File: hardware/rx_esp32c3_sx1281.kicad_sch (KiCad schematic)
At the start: 43 parts, among them U21 SX1281IMLTRT, U22 ESP32-C3, U23 TLV75533PDQNR, X2 CJ17-400001010B20

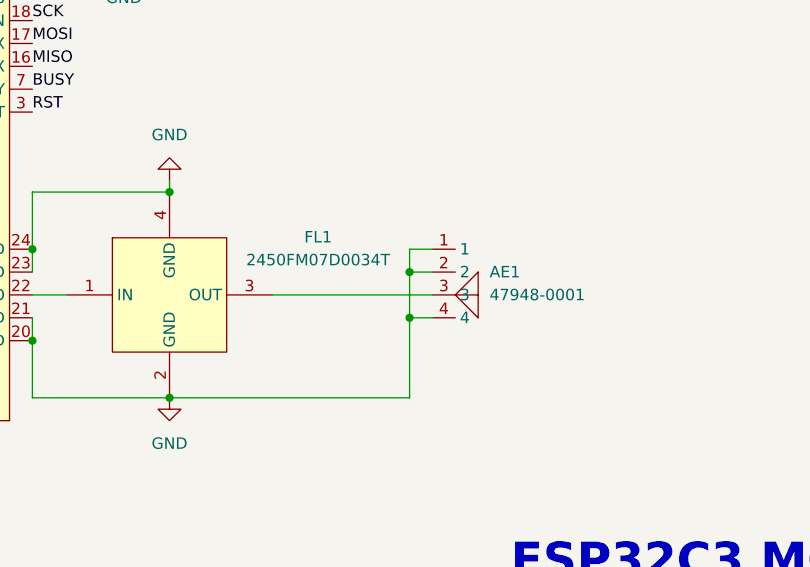
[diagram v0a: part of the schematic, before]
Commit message: Base: routing progress (~60%), netclass clearances relaxed
VBAT/Phase/Power/RF clearance lowered toward the 0.09 line standard; the
2 oz outer rule in the DRU still enforces 0.16 on F/B.Cu. Schematic sheets
resaved by eeschema, no circuit change.
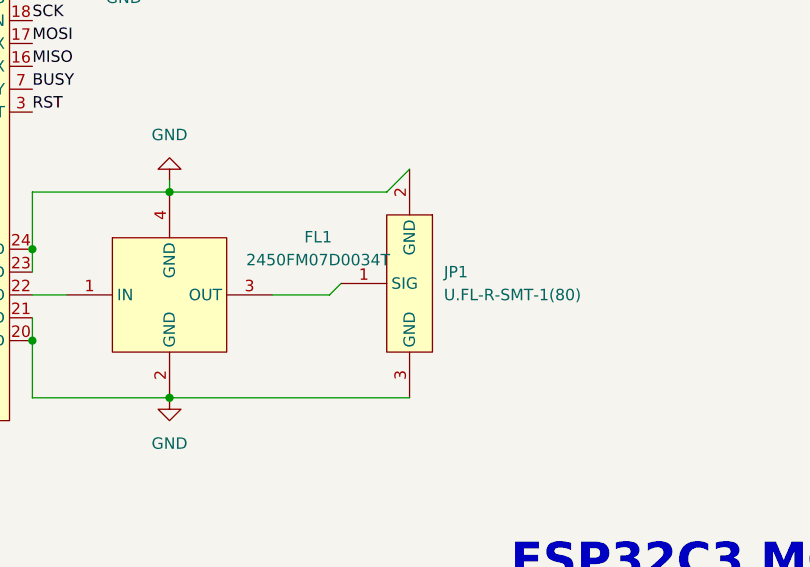
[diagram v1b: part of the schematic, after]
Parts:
- removed AE1: 47948-0001, OpenRX-Shared:ANT-SMD_47948-0001, symbol OpenRX-Shared:47948-0001
- added JP1: U.FL-R-SMT-1(80), OpenDrone:RF-SMD_FRF05002-JSS103M, symbol OpenDrone:U.FL-R-SMT-1(80)
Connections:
- net GND: now also JP1.2 (GND), JP1.3 (GND)
- net at FL1.3 (OUT): now also JP1.1 (SIG)
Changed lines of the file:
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@@
 	)
 	(junction
-		(at 185.42 119.38)
-		(diameter 0)
-		(color 0 0 0 0)
-	)
-	(junction
 		(at 273.05 93.98)
 		(diameter 0)
@@
 	)
 	(junction
-		(at 185.42 114.3)
-		(diameter 0)
-		(color 0 0 0 0)
-	)
-	(junction
 		(at 91.44 81.28)
 		(diameter 0)
@@
 	(wire
 		(pts
-			(xy 170.18 116.84) (xy 187.96 116.84)
-		)
-		(stroke
-			(width 0)
-			(type default)
-		)
-	)
-	(wire
-		(pts
 			(xy 279.4 93.98) (xy 279.4 96.52)
 		)
@@
 	(wire
 		(pts
-			(xy 185.42 114.3) (xy 185.42 119.38)
-		)
-		(stroke
-			(width 0)
-			(type default)
-		)
-	)
-	(wire
-		(pts
 			(xy 167.64 233.68) (xy 199.39 233.68)
 		)
@@
 	(wire
 		(pts
+			(xy 158.75 105.41) (xy 182.88 105.41)
+		)
+		(stroke
+			(width 0)
+			(type default)
+		)
+	)
+	(wire
+		(pts
 			(xy 77.47 71.12) (xy 80.01 71.12)
 		)
@@
 	(wire
 		(pts
+			(xy 170.18 116.84) (xy 176.53 116.84)
+		)
+		(stroke
+			(width 0)
+			(type default)
+		)
+	)
+	(wire
+		(pts
 			(xy 273.05 93.98) (xy 273.05 95.25)
 		)
@@
 	(wire
 		(pts
-			(xy 185.42 119.38) (xy 185.42 128.27)
-		)
-		(stroke
-			(width 0)
-			(type default)
-		)
-	)
-	(wire
-		(pts
 			(xy 212.09 195.58) (xy 212.09 179.07)
 		)
@@
 	(wire
 		(pts
-			(xy 261.62 93.98) (xy 273.05 93.98)
+			(xy 182.88 105.41) (xy 185.42 102.87)
 		)
 		(stroke
@@
 	(wire
 		(pts
-			(xy 264.16 180.34) (xy 264.16 179.07)
+			(xy 261.62 93.98) (xy 273.05 93.98)
 		)
 		(stroke
@@
 	(wire
 		(pts
-			(xy 187.96 111.76) (xy 185.42 111.76)
+			(xy 264.16 180.34) (xy 264.16 179.07)
 		)
 		(stroke
@@
 	(wire
 		(pts
-			(xy 187.96 114.3) (xy 185.42 114.3)
+			(xy 273.05 104.14) (xy 287.02 104.14)
 		)
 		(stroke
@@
 	(wire
 		(pts
-			(xy 273.05 104.14) (xy 287.02 104.14)
+			(xy 303.53 104.14) (xy 303.53 102.87)
 		)
 		(stroke
@@
 	(wire
 		(pts
-			(xy 303.53 104.14) (xy 303.53 102.87)
+			(xy 107.95 71.12) (xy 91.44 71.12)
 		)
 		(stroke
@@
 	(wire
 		(pts
-			(xy 107.95 71.12) (xy 91.44 71.12)
+			(xy 245.11 215.9) (xy 254 215.9)
 		)
 		(stroke
@@
 	(wire
 		(pts
-			(xy 245.11 215.9) (xy 254 215.9)
+			(xy 83.82 104.14) (xy 83.82 116.84)
 		)
 		(stroke
@@
 	(wire
 		(pts
-			(xy 83.82 104.14) (xy 83.82 116.84)
+			(xy 176.53 116.84) (xy 177.8 115.57)
 		)
 		(stroke
@@
 	(wire
 		(pts
-			(xy 185.42 111.76) (xy 185.42 114.3)
-		)
-		(stroke
-			(width 0)
-			(type default)
-		)
-	)
-	(wire
-		(pts
 			(xy 261.62 95.25) (xy 261.62 93.98)
 		)
@@
 	(wire
 		(pts
-			(xy 185.42 119.38) (xy 187.96 119.38)
-		)
-		(stroke
-			(width 0)
-			(type default)
-		)
-	)
-	(wire
-		(pts
 			(xy 181.61 186.69) (xy 168.91 186.69)
 		)
@@
 	)
 	(symbol
+		(lib_id "OpenDrone:U.FL-R-SMT-1(80)")
+		(at 182.88 115.57 270)
+		(unit 1)
+		(body_style 1)
+		(exclude_from_sim no)
+		(in_bom yes)
+		(on_board yes)
+		(in_pos_files yes)
+		(dnp no)
+		(fields_autoplaced yes)
+		(property "Reference" "JP1"
+			(at 189.23 114.2999 90)
+			(show_name no)
+			(do_not_autoplace no)
+			(effects
+				(font
+					(size 1.27 1.27)
+				)
+				(justify left)
+			)
+		)
+		(property "Value" "U.FL-R-SMT-1(80)"
+			(at 189.23 116.8399 90)
+			(show_name no)
+			(do_not_autoplace no)
+			(effects
+				(font
+					(size 1.27 1.27)
+				)
+				(justify left)
+			)
+		)
+		(property "Footprint" "OpenDrone:RF-SMD_FRF05002-JSS103M"
+			(at 170.18 115.57 0)
+			(hide yes)
+			(show_name no)
+			(do_not_autoplace no)
+			(effects
+				(font
+					(size 1.27 1.27)
+				)
+			)
+		)
+		(property "Datasheet" "https://lcsc.com/product-detail/Connectors_HRS_U-FL-R-SMT-1-80_3310472280-IPE-XBoard-end-IPXConnector-SMD_C88374.html"
+			(at 167.64 115.57 0)
+			(hide yes)
+			(show_name no)
+			(do_not_autoplace no)
+			(effects
+				(font
+					(size 1.27 1.27)
+				)
+			)
+		)
+		(property "Description" ""
+			(at 182.88 115.57 0)
+			(hide yes)
+			(show_name no)
+			(do_not_autoplace no)
+			(effects
+				(font
+					(size 1.27 1.27)
+				)
+			)
+		)
+		(property "LCSC Part" "C88374"
+			(at 165.1 115.57 0)
+			(hide yes)
+			(show_name no)
+			(do_not_autoplace no)
+			(effects
+				(font
+					(size 1.27 1.27)
+				)
+			)
+		)
+		(pin "3"
+		)
+		(pin "2"
+		)
+		(pin "1"
+		)
+		(instances
+			(project "OpenAIO-Base"
+				(path "/fb88b6f9-ee39-4640-a9d4-04a17ceeac64/6e8501c6-71d5-4860-9b96-3d3562c097af"
+					(reference "JP1")
+					(unit 1)
+				)
+			)
+		)
+	)
+	(symbol
 		(lib_id "power:GND")
 		(at 109.22 59.69 0)
@@
 					(unit 1)
 				)
-			)
-		)
-	)
-	(symbol
-		(lib_id "OpenRX-Shared:47948-0001")
-		(at 190.5 116.84 270)
-		(unit 1)
-		(body_style 1)
-		(exclude_from_sim no)
-		(in_bom yes)
-		(on_board yes)
-		(in_pos_files yes)
-		(dnp no)
-		(fields_autoplaced yes)
-		(property "Reference" "AE1"
-			(at 194.31 114.2999 90)
-			(show_name no)
-			(do_not_autoplace no)
-			(effects
-				(font
-					(size 1.27 1.27)
-				)
-				(justify left)
-			)
-		)
-		(property "Value" "47948-0001"
-			(at 194.31 116.8399 90)
-			(show_name no)
-			(do_not_autoplace no)
-			(effects
-				(font
-					(size 1.27 1.27)
-				)
-				(justify left)
-			)
-		)
-		(property "Footprint" "OpenRX-Shared:ANT-SMD_47948-0001"
-			(at 180.34 116.84 0)
-			(hide yes)
-			(show_name no)
-			(do_not_autoplace no)
-			(effects
-				(font
-					(size 1.27 1.27)
-				)
-			)
-		)
-		(property "Datasheet" "https://lcsc.com/product-detail/RF-Antenna_MOLEX_47948-0001_47948-0001_C152351.html"
-			(at 177.8 116.84 0)
-			(hide yes)
-			(show_name no)
-			(do_not_autoplace no)
-			(effects
-				(font
-					(size 1.27 1.27)
-				)
-			)
-		)
-		(property "Description" ""
-			(at 190.5 116.84 0)
-			(hide yes)
-			(show_name no)
-			(do_not_autoplace no)
-			(effects
-				(font
-					(size 1.27 1.27)
-				)
-			)
-		)
-		(property "LCSC Part" "C152351"
-			(at 175.26 116.84 0)
-			(hide yes)
-			(show_name no)
-			(do_not_autoplace no)
-			(effects
-				(font
-					(size 1.27 1.27)
-				)
-			)
-		)
-		(pin "4"
-		)
-		(pin "1"
-		)
-		(pin "3"
-		)
-		(pin "2"
-		)
-		(instances
-			(project "OpenRX-Lite"
-				(path "/8521861a-4fab-458b-8289-5e2efb91d906/d4225140-81df-42e7-abd7-e679e5ab5187"
-					(reference "AE2")
-					(unit 1)
-				)
-			)
-			(project "OpenAIO-Base"
-				(path "/fb88b6f9-ee39-4640-a9d4-04a17ceeac64/6e8501c6-71d5-4860-9b96-3d3562c097af"
-					(reference "AE1")
-					(unit 1)
-				)
